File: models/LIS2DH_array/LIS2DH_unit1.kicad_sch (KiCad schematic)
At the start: 5 parts, among them U1 LIS2DH12TR, U17 SN74LVC1G32DCKR

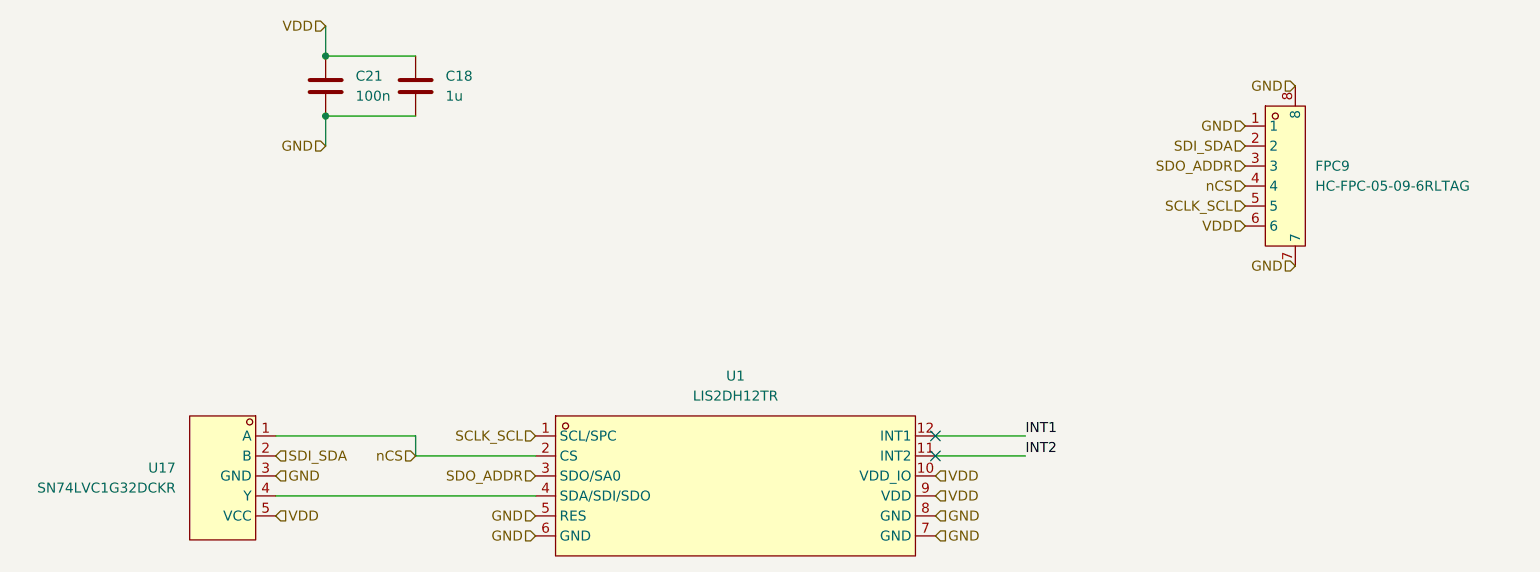
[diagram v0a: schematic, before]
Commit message: updated lis2dh arrays
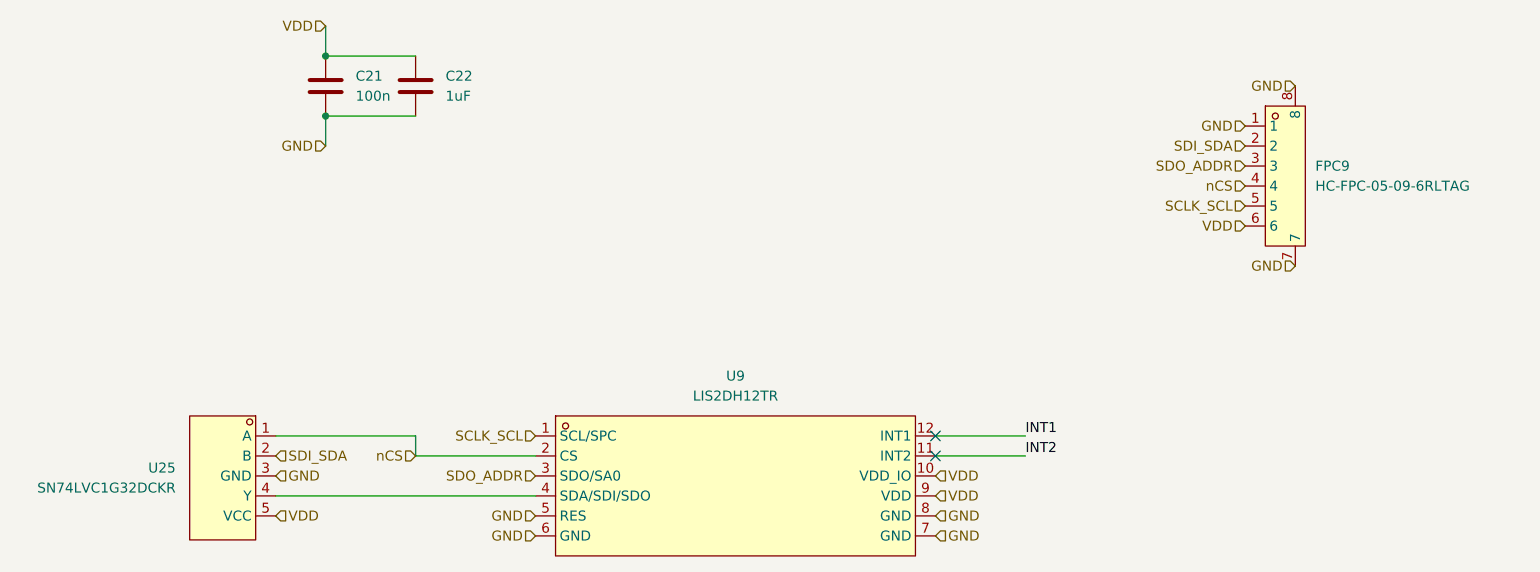
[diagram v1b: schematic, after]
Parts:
- C21: LCSC Part (none) -> C1525
- C22: renamed from C18; value 1u -> 1uF; LCSC Part (none) -> C52923
- renumbered U17 to U25, U1 to U9
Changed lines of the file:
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@@
 		(dnp no)
 		(fields_autoplaced yes)
-		(property "Reference" "U1"
+		(property "Reference" "U9"
 			(at 116.84 119.38 0)
 			(effects
@@
 		(dnp no)
 		(fields_autoplaced yes)
-		(property "Reference" "C18"
+		(property "Reference" "C22"
 			(at 80.01 81.2799 0)
 			(effects
@@
 			)
 		)
-		(property "Value" "1u"
+		(property "Value" "1uF"
 			(at 80.01 83.8199 0)
 			(effects
@@
 		)
 		(property "Description" ""
+			(at 76.2 82.55 0)
+			(effects
+				(font
+					(size 1.27 1.27)
+				)
+				(hide yes)
+			)
+		)
+		(property "LCSC Part" "C52923 "
 			(at 76.2 82.55 0)
 			(effects
@@
 			)
 		)
+		(property "LCSC Part" "C1525"
+			(at 64.77 82.55 0)
+			(effects
+				(font
+					(size 1.27 1.27)
+				)
+				(hide yes)
+			)
+		)
 		(pin "1"
 		)
@@
 		(dnp no)
 		(fields_autoplaced yes)
-		(property "Reference" "U17"
+		(property "Reference" "U25"
 			(at 45.72 131.0649 0)
 			(effects
